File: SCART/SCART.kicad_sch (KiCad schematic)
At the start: 3 parts, among them J1 Socket, J2 Ground, J3 Breakout

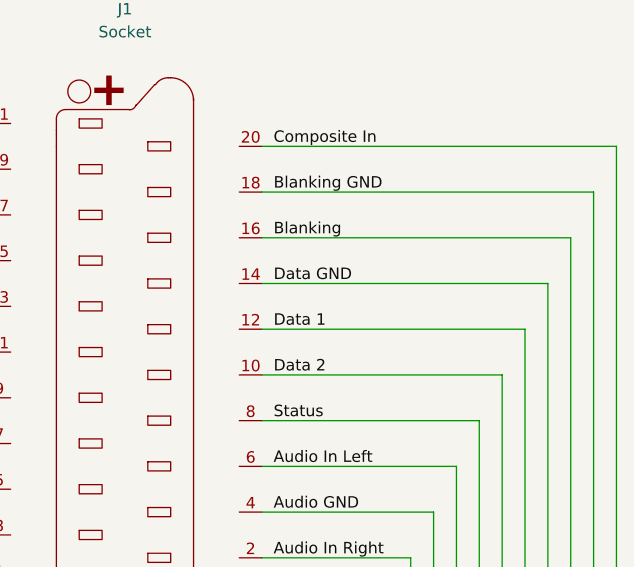
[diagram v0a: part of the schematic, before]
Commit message: Finish SCART board.
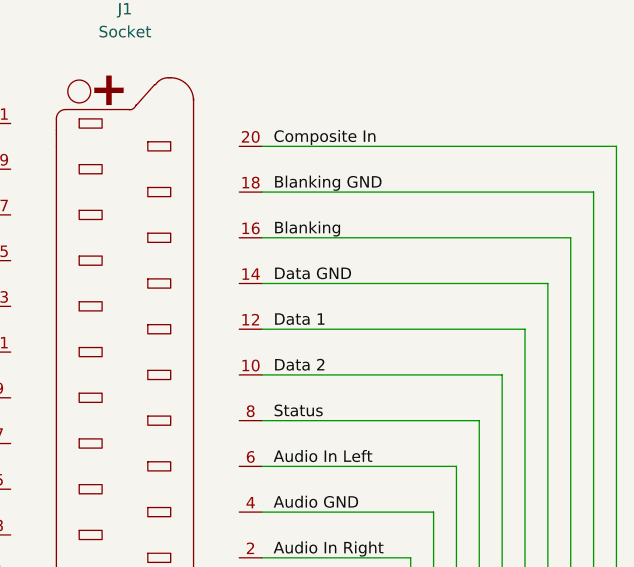
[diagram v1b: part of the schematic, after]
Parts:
- J1: footprint (none) -> T-Pau:SCART
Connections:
- net Data GND: now also J1.14 (P14)
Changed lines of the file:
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@@
+	(wire
+		(pts
+			(xy 151.13 50.8) (xy 182.88 50.8)
+		)
+		(stroke
+			(width 0)
+			(type default)
+		)
+	)
 	(wire
 		(pts
@@
 		(pts
 			(xy 142.24 109.22) (xy 172.72 109.22)
-		)
-		(stroke
-			(width 0)
-			(type default)
-		)
-	)
-	(wire
-		(pts
-			(xy 151.1374 50.8) (xy 182.88 50.8)
 		)
 		(stroke
@@
 			)
 		)
-		(property "Footprint" ""
+		(property "Footprint" "T-Pau:SCART"
 			(at 135.89 57.15 0)
 			(effects
